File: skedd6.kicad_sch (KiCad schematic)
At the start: 12 parts, among them J1 Conn_02x10_Odd_Even, J2 Conn_02x03_Odd_Even, J3 Conn_01x03_Pin, J4 Conn_01x03_Pin, J5 Conn_01x02_Pin, J6 Conn_01x02_Pin, U1 AMS1117-3.3

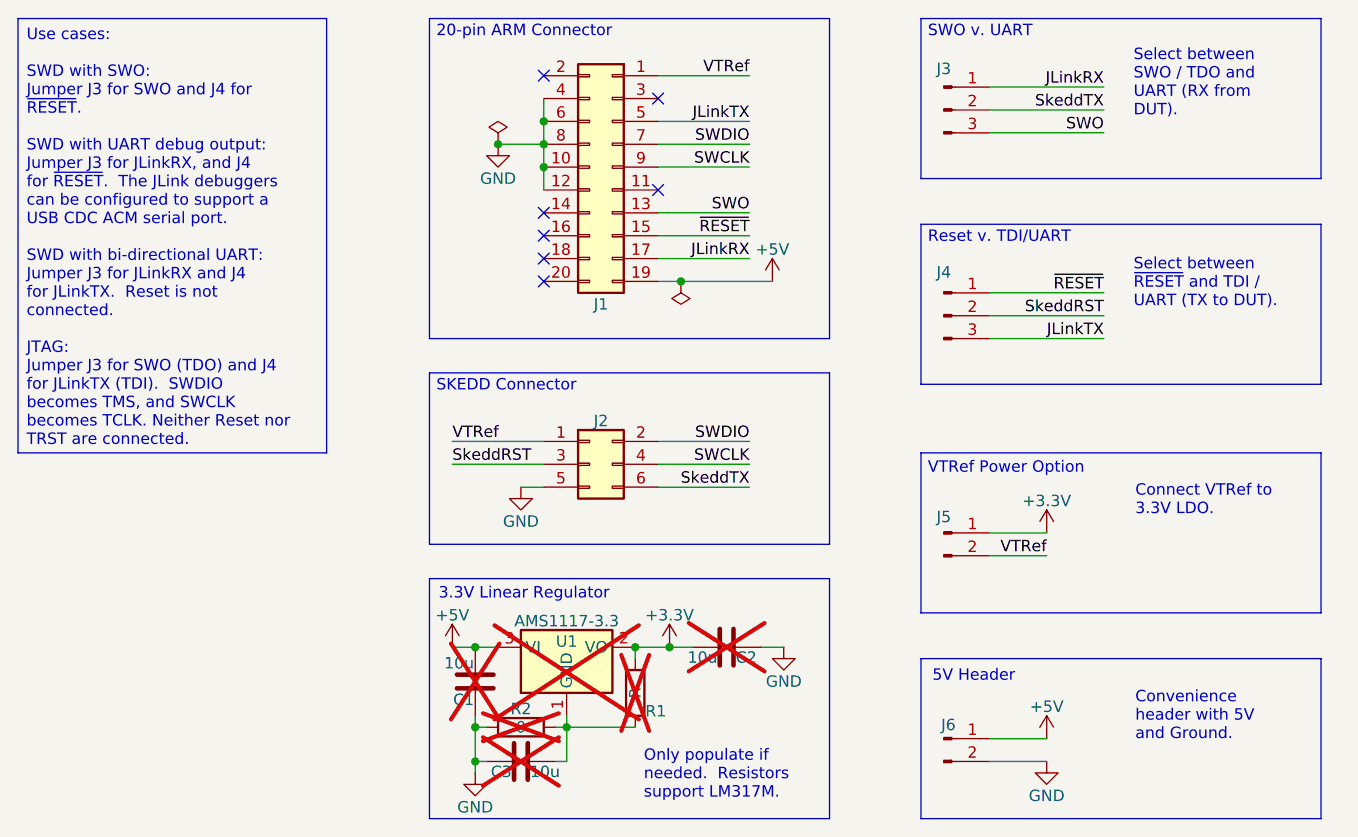
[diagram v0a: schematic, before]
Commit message: Version with AP7362 LDO
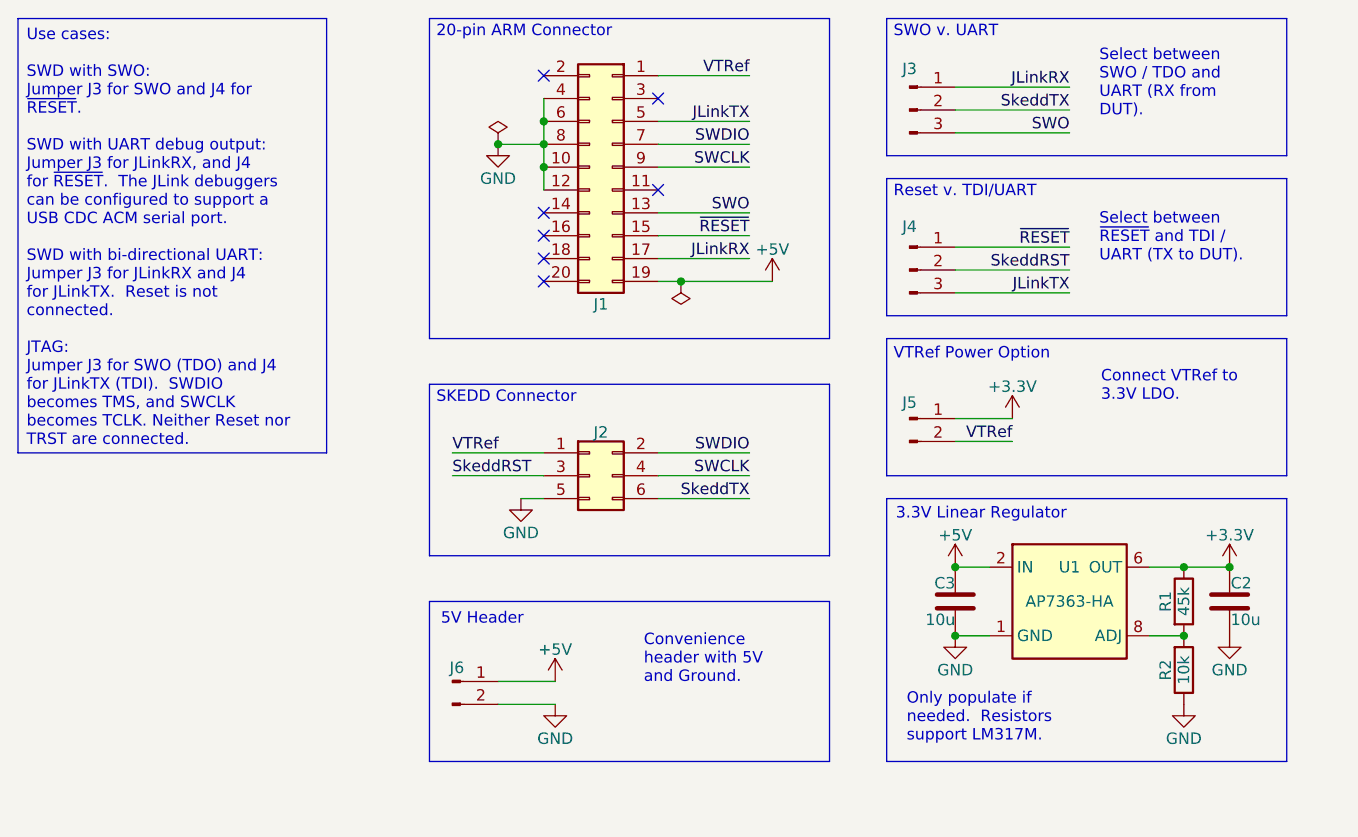
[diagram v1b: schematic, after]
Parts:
- removed C1: 10u, Capacitor_SMD:C_0603_1608Metric, symbol Device:C
- removed U1: AMS1117-3.3, Parts:SOT-223-3_TabPin2, symbol Regulator_Linear:AMS1117-3.3
- added U1: AP7363-HA, Parts:DFN-8-1EP_3x2mm_P0.5mm_EP1.6x1.5mm, symbol Parts:AP7363C-HA
- C2, C3: now fitted
- R1: value R -> 45k; now fitted
- R2: value 0 -> 10k; now fitted
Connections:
- net +3.3V: now also C2.2, U1.5 (OUT), U1.6 (OUT), U1.7 (OUT); no longer C2.1
- net +5V: now also C3.2, U1.2 (IN), U1.3 (IN), U1.4 (IN)
- net GND: now also C2.1, U1.1 (GND), U1.9 (GND); no longer C2.2
- net at R1.2, R2.2: now also U1.8 (ADJ); no longer C3.2
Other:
- moved on the sheet: J2, J3, J4, J5, J6
